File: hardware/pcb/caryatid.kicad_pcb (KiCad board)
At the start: 2 copper layers, 100 x 90 mm, 129 parts, among them J1 DC in, J10 FSR, J11 Digital bus, J12 RGB status, J13A Comms A - Qwiic, J13B Comms A - module, J14 Mic bias return, J15 Comms B - module, J16 Expansion / SPI1, J17 Audio out L/R/G, J18 Audio in L/R/rtn, J2 Battery, remote, J3 Latch switch, J4 Charge LEDs, J5 Analogue bus, J6 SW1 switch, J7 SW2 switch, J8 SW3 switch, J9 Soft pot, U1 BQ24074RGT, U2 TPS61023DRL, U3 74HC14, U4 MCP6002

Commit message: Hide back references, scope a clearance override to U1 and U2
Back-side designators hidden: 104 SMD parts at this density made them illegible
and they collided 87 times. JLC places from the CPL, not from silkscreen. Front
designators stay -- that face is sparse and is what a human cables up.

U1 and U2 get a footprint-level 0.15 mm clearance override. A 0.5 mm pitch
package fixes its own pad gaps and the HighCurrent netclass asks 0.3 mm, which
no land pattern at that pitch can meet. Scoped to the two packages; traces still
answer to their netclass.

Zone overflow now goes to the rescue pass rather than running off the board, and
the rescue pass keeps 3 mm of edge margin. R6, R9 and R10 were rescued; R10 had
been sitting exactly on the bottom edge.

Two bugs in my own insertion code, both of which produced a file that balanced
but was structurally wrong: the (hide yes) regex matched the closing paren of
the nested (font ...) rather than (effects ...), burying the flag inside the
font; and the clearance override silently matched nothing. Both replaced with
balanced-paren parsing.

silk_overlap 92 -> 5, clearance 18 -> 4, copper_edge_clearance 4 -> 0.
Non-ratsnest violations 133 -> 14.
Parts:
- moved R10 66.1 mm to (80.5, 56.5)
- moved R9 63.5 mm to (58.5, 56.5)
- moved R6 61.7 mm to (54.5, 56.5)

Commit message: Ground pour on F.Cu, and the boost hot loop
A GND zone on F.Cu, which that face can carry as a near-solid plane because it
holds only 21 through-hole parts. The zone ships unfilled -- kicad-cli has no
fill option -- so DRC reports the two GND vias as dangling until zones are
filled in the editor.

The hot loop: +5V_RAW from U2 pin 6 to C6 at 0.8 mm, and the return taken into
the plane by a via at each ground pad rather than by a track, so the return runs
directly under the outgoing current.

Two mistakes worth recording. A track wider than the pad pitch shorts to the
neighbouring pad -- 0.8 mm centred on pin 6 overlapped pin 5 -- so exits from
0.5 mm-pitch pads now neck to 0.25 mm and widen once clear. And via positions
are now searched against every back-side pad: the first attempt put a GND via
through C7's +5V pad, because I had checked it against the boost cluster only.

SW is left unrouted. U2 pin 5 can only exit right and C6 occupies that gap, so
there is no path to L1 at a useful width. That is placement, not routing: this
cluster has room for either the tight hot loop or the short SW node, not both.
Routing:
- net VOUT: track 0.00 -> 3.97 mm
- net +5V_RAW: track 0.00 -> 1.84 mm
- net GND: track 0.00 -> 1.00 mm, vias 0 -> 2
- added copper zone on F.Cu, net GND
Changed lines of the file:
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@@
+		)
+	)
+	(segment
+		(start 64.713 104.5)
+		(end 65.6 104.5)
+		(width 0.25)
+		(layer "B.Cu")
+		(net 4)
+	)
+	(segment
+		(start 65.6 104.5)
+		(end 66.55 104.5)
+		(width 0.8)
+		(layer "B.Cu")
+		(net 4)
+	)
+	(segment
+		(start 63.288 103.5)
+		(end 62.4 103.5)
+		(width 0.25)
+		(layer "B.Cu")
+		(net 94)
+	)
+	(segment
+		(start 62.4 103.5)
+		(end 61.45 103.5)
+		(width 1.2)
+		(layer "B.Cu")
+		(net 94)
+	)
+	(segment
+		(start 66.475 100.0)
+		(end 68.55 100.5)
+		(width 1.2)
+		(layer "B.Cu")
+		(net 94)
+	)
+	(segment
+		(start 68.45 104.5)
+		(end 68.95 104.5)
+		(width 0.25)
+		(layer "B.Cu")
+		(net 91)
+	)
+	(via
+		(at 68.95 104.5)
+		(size 0.6)
+		(drill 0.3)
+		(layers "F.Cu" "B.Cu")
+		(net 91)
+	)
+	(segment
+		(start 64.713 103.5)
+		(end 64.28 103.25)
+		(width 0.25)
+		(layer "B.Cu")
+		(net 91)
+	)
+	(via
+		(at 64.28 103.25)
+		(size 0.6)
+		(drill 0.3)
+		(layers "F.Cu" "B.Cu")
+		(net 91)
+	)
+	(zone
+		(net 91)
+		(net_name "GND")
+		(layer "F.Cu")
+		(name "GND plane")
+		(hatch edge 0.5)
+		(connect_pads
+			(clearance 0.3)
+		)
+		(min_thickness 0.25)
+		(filled_areas_thickness no)
+		(fill yes
+			(thermal_gap 0.3)
+			(thermal_bridge_width 0.5)
+		)
+		(polygon
+			(pts
+				(xy 50.6 30.6) (xy 149.4 30.6) (xy 149.4 119.4) (xy 50.6 119.4)
+			)
 		)
 	)

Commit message: Move C6 below U2 so SW routes
Putting the output cap beside U2 was the obvious spot and it quietly cost the
switching node: pin 5 can only exit right and C6 was standing in that gap. C6
now sits below U2, which frees the right side for L1 and, because pin 6 is on
the near edge either way, barely lengthens the hot loop.

  hot loop  1.84 -> 2.01 mm
  SW node   4.17 mm unroutable -> 2.31 mm, routed at 1.2 mm

Trading 0.17 mm of hot loop for a routable 1.5 A switching node is not close.
The general lesson is that routability is a placement constraint: optimising
loop length without it produced an arrangement that measured well and could not
be built.

Three power pins leave a 0.5 mm-pitch package into a 1.5 mm band, so every exit
necks to 0.2 mm and widens once clear of the pads. With that the routing adds no
DRC violations of its own -- the four clearance items are the pre-existing
SOT-563 pad-pitch ones against the 0.2 mm board floor.
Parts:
- moved R10 45.6 mm to (77.5, 102.0)
- moved R6 40.7 mm to (72.5, 93.0)
- moved R9 40.7 mm to (76.5, 93.0)
- moved R5 20.5 mm to (68.5, 93.0)
- moved C7 15.9 mm to (61.5, 96.0)
- moved FB1 8.32 mm to (64.5, 109.0)
- moved L1 5.32 mm to (68.5, 104.0)
- moved C5 4.95 mm to (73.0, 104.0)
- moved C6 4.03 mm to (64.0, 106.5), turned to 180 degrees
- moved R7 1.00 mm to (60.0, 106.5)
- moved R8 1.00 mm to (60.0, 108.5)
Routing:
- net /power/SW: track 0.00 -> 2.31 mm
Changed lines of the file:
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@@
 	(footprint "Capacitor_SMD:C_0805_2012Metric"
 		(layer "B.Cu")
-		(at 69.5 100.5)
+		(at 73.0 104.0)
 		(descr "Capacitor SMD 0805 (2012 Metric), square (rectangular) end terminal, IPC-7351 nominal, (Body size source: IPC-SM-782 page 76, https://www.pcb-3d.com/wordpress/wp-content/uploads/ipc-sm-782a_amendment_1_and_2.pdf, https://docs.google.com/spreadsheets/d/1BsfQQcO9C6DZCsRaXUlFlo91Tg2WpOkGARC1WS5S8t0/edit?usp=sharing), generated with kicad-footprint-generator")
 		(tags "capacitor")
@@
 	(footprint "Capacitor_SMD:C_0805_2012Metric"
 		(layer "B.Cu")
-		(at 67.5 104.5)
+		(at 64.0 106.5 180)
 		(descr "Capacitor SMD 0805 (2012 Metric), square (rectangular) end terminal, IPC-7351 nominal, (Body size source: IPC-SM-782 page 76, https://www.pcb-3d.com/wordpress/wp-content/uploads/ipc-sm-782a_amendment_1_and_2.pdf, https://docs.google.com/spreadsheets/d/1BsfQQcO9C6DZCsRaXUlFlo91Tg2WpOkGARC1WS5S8t0/edit?usp=sharing), generated with kicad-footprint-generator")
 		(tags "capacitor")
@@
 	(footprint "Capacitor_SMD:CP_Elec_6.3x5.4"
 		(layer "B.Cu")
-		(at 73.0 107.0)
+		(at 61.5 96.0)
 		(descr "SMD capacitor, aluminum electrolytic, Panasonic C55, 6.3x5.4mm")
 		(tags "capacitor electrolytic")
@@
 	(footprint "Inductor_SMD:L_0805_2012Metric"
 		(layer "B.Cu")
-		(at 71.5 104.5)
+		(at 64.5 109.0)
 		(descr "Inductor SMD 0805 (2012 Metric), square (rectangular) end terminal, IPC-7351 nominal, (Body size source: IPC-SM-782 page 80, https://www.pcb-3d.com/wordpress/wp-content/uploads/ipc-sm-782a_amendment_1_and_2.pdf), generated with kicad-footprint-generator")
 		(tags "inductor")
@@
 	(footprint "Inductor_SMD:L_Vishay_IFSC-1515AH_4x4x1.8mm"
 		(layer "B.Cu")
-		(at 65.0 100.0 180)
+		(at 68.5 104.0 180)
 		(descr "Low Profile, High Current Inductors (https://www.vishay.com/docs/34295/sc15ah01.pdf)")
 		(tags "SMD Vishay Inductor Low Profile")
@@
 	(footprint "Resistor_SMD:R_0603_1608Metric"
 		(layer "B.Cu")
-		(at 80.5 56.5)
+		(at 77.5 102.0)
 		(descr "Resistor SMD 0603 (1608 Metric), square (rectangular) end terminal, IPC-7351 nominal, (Body size source: IPC-SM-782 page 72, https://www.pcb-3d.com/wordpress/wp-content/uploads/ipc-sm-782a_amendment_1_and_2.pdf), generated with kicad-footprint-generator")
 		(tags "resistor")
@@
 	(footprint "Resistor_SMD:R_0603_1608Metric"
 		(layer "B.Cu")
-		(at 69.0 113.5)
+		(at 68.5 93.0)
 		(descr "Resistor SMD 0603 (1608 Metric), square (rectangular) end terminal, IPC-7351 nominal, (Body size source: IPC-SM-782 page 72, https://www.pcb-3d.com/wordpress/wp-content/uploads/ipc-sm-782a_amendment_1_and_2.pdf), generated with kicad-footprint-generator")
 		(tags "resistor")
@@
 	(footprint "Resistor_SMD:R_0603_1608Metric"
 		(layer "B.Cu")
-		(at 54.5 56.5)
+		(at 72.5 93.0)
 		(descr "Resistor SMD 0603 (1608 Metric), square (rectangular) end terminal, IPC-7351 nominal, (Body size source: IPC-SM-782 page 72, https://www.pcb-3d.com/wordpress/wp-content/uploads/ipc-sm-782a_amendment_1_and_2.pdf), generated with kicad-footprint-generator")
 		(tags "resistor")
@@
 	(footprint "Resistor_SMD:R_0603_1608Metric"
 		(layer "B.Cu")
-		(at 61.0 106.5)
+		(at 60.0 106.5)
 		(descr "Resistor SMD 0603 (1608 Metric), square (rectangular) end terminal, IPC-7351 nominal, (Body size source: IPC-SM-782 page 72, https://www.pcb-3d.com/wordpress/wp-content/uploads/ipc-sm-782a_amendment_1_and_2.pdf), generated with kicad-footprint-generator")
 		(tags "resistor")
@@
 	(footprint "Resistor_SMD:R_0603_1608Metric"
 		(layer "B.Cu")
-		(at 61.0 108.5)
+		(at 60.0 108.5)
 		(descr "Resistor SMD 0603 (1608 Metric), square (rectangular) end terminal, IPC-7351 nominal, (Body size source: IPC-SM-782 page 72, https://www.pcb-3d.com/wordpress/wp-content/uploads/ipc-sm-782a_amendment_1_and_2.pdf), generated with kicad-footprint-generator")
 		(tags "resistor")
@@
 	(footprint "Resistor_SMD:R_0603_1608Metric"
 		(layer "B.Cu")
-		(at 58.5 56.5)
+		(at 76.5 93.0)
 		(descr "Resistor SMD 0603 (1608 Metric), square (rectangular) end terminal, IPC-7351 nominal, (Body size source: IPC-SM-782 page 72, https://www.pcb-3d.com/wordpress/wp-content/uploads/ipc-sm-782a_amendment_1_and_2.pdf), generated with kicad-footprint-generator")
 		(tags "resistor")
@@
 	(segment
 		(start 64.713 104.5)
-		(end 65.6 104.5)
-		(width 0.25)
+		(end 64.713 105.5)
+		(width 0.2)
 		(layer "B.Cu")
 		(net 4)
 	)
 	(segment
-		(start 65.6 104.5)
-		(end 66.55 104.5)
+		(start 64.713 105.5)
+		(end 64.95 106.5)
 		(width 0.8)
 		(layer "B.Cu")
@@
 	)
 	(segment
+		(start 64.713 104.0)
+		(end 66.4 104.0)
+		(width 0.2)
+		(layer "B.Cu")
+		(net 50)
+	)
+	(segment
+		(start 66.4 104.0)
+		(end 67.025 104.0)
+		(width 1.2)
+		(layer "B.Cu")
+		(net 50)
+	)
+	(segment
 		(start 63.288 103.5)
-		(end 62.4 103.5)
-		(width 0.25)
+		(end 61.9 103.5)
+		(width 0.2)
 		(layer "B.Cu")
 		(net 94)
 	)
 	(segment
-		(start 62.4 103.5)
+		(start 61.9 103.5)
 		(end 61.45 103.5)
 		(width 1.2)
@@
 	)
 	(segment
-		(start 66.475 100.0)
-		(end 68.55 100.5)
+		(start 69.975 104.0)
+		(end 72.05 104.0)
 		(width 1.2)
 		(layer "B.Cu")
@@
 	)
 	(segment
-		(start 68.45 104.5)
-		(end 68.95 104.5)
-		(width 0.25)
+		(start 63.05 106.5)
+		(end 63.55 106.5)
+		(width 0.2)
 		(layer "B.Cu")
 		(net 91)
 	)
 	(via
-		(at 68.95 104.5)
+		(at 63.55 106.5)
 		(size 0.6)
 		(drill 0.3)
@@
 		(start 64.713 103.5)
 		(end 64.28 103.25)
-		(width 0.25)
+		(width 0.2)
 		(layer "B.Cu")
 		(net 91)

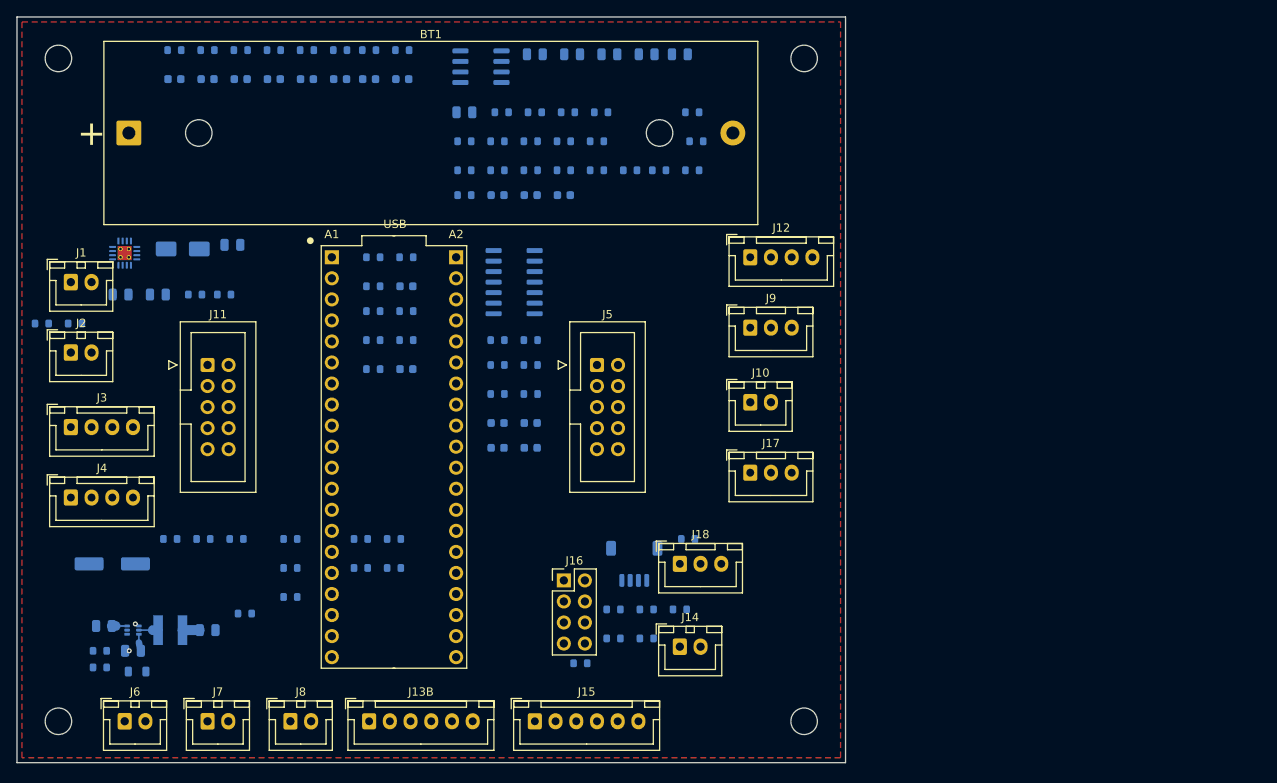
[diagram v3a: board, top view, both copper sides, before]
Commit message: Board to 150 x 90, and a checker for the constraints DRC misses
The recurring failure this session was always the same shape: a check that
modelled one thing and silently ignored another. tools/check_board.py now
enumerates all eight classes in one re-runnable pass -- courtyard overlap per
face INCLUDING the mounting holes, back parts over front through-hole pads,
outline margin, component height vs standoff, via annular ring, track width vs
pad pitch, and silkscreen against the fab floors. Four of those have no
equivalent in KiCad's DRC as configured, which is why they were all missed.

Outline 90 x 100 -> 150 x 90. Coverage 50% -> 33%, perimeter 380 -> 480 mm,
which matters because an early commit identified the perimeter rather than the
area as binding. All growth is on the long axis where the conservative BUD
rectangle leaves 15 mm; the 90 mm axis is untouched because it is the one proven
to fit. 100 x 150 was in the approved plan and is NOT what was built -- 100
exceeds the documented 95.2 mm BUD width, which the plan failed to check.

Three DRC rules were set looser than the fab and reported false passes:
min_via_annular_width 0.13 -> 0.18, min_hole_to_hole 0.25 -> 0.45. min_clearance
0.20 -> 0.15, still 1.5x JLC's 0.10, which retires the four SOT-563 clearance
errors caused by its own pad pitch.

Via pads 0.55/0.6 -> 0.70 on 0.3 drill for a 0.20 mm ring; QFN thermal vias
inboard to +/-0.45 so the larger pad still clears the signal pads by 0.25 mm.

Standoffs are 7 mm, set by C7 at 5.4 mm on the back face. The height was never
specified and 4-5 mm does not clear it -- found by the user, not by me, which is
why the height check now exists.

ADR 0008 records the outline and layer count, which were never written up
despite ADR 0001's own criterion. It also retires the 'neither edge past 100 mm'
rule: the price tier is real but the cost of crossing it was never checked, and
checking it showed the increase is small.

DRC non-ratsnest 14 -> 10. ERC 0. Pin map unchan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
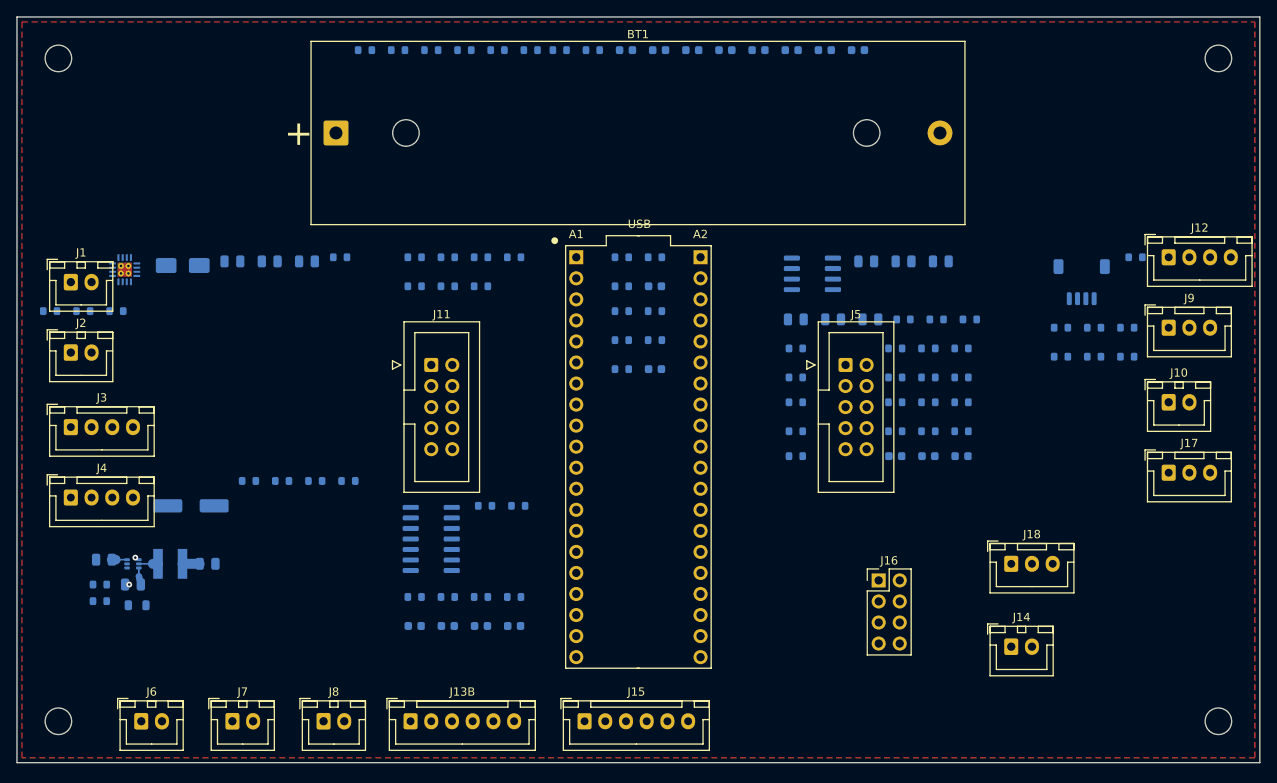
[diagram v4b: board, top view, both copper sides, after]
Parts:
- moved R46 75.7 mm to (184.0, 71.0)
- moved J13A 63.8 mm to (178.5, 62.0)
- moved R40 63.8 mm to (185.0, 59.0)
- moved R41 63.8 mm to (176.0, 67.5)
- moved R42 63.8 mm to (180.0, 67.5)
- moved R43 63.8 mm to (184.0, 67.5)
- moved R44 63.8 mm to (176.0, 71.0)
- moved R45 63.8 mm to (180.0, 71.0)
- moved R52 61.3 mm to (160.0, 70.0)
- moved R53 61.3 mm to (164.0, 70.0)
- moved C23 57.4 mm to (156.0, 83.0)
- moved C27 57.4 mm to (160.0, 83.0)
- moved C30 57.4 mm to (164.0, 83.0)
- moved R59 55.6 mm to (156.0, 76.5)
- moved R60 55.6 mm to (160.0, 76.5)
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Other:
- board size 100 x 90 mm -> 150 x 90 mm
- board text added: "caryatid 150 x 90 mm 2 layer"
- board text removed: "caryatid 90 x 100 mm 2 layer"

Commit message: Everything to the front; ground plane to B.Cu; standoff 2 mm
The enclosure is shallow, so the standoff has to be short, and C7 at 5.4 mm
cannot hang under it. Rather than move the tall parts individually, every
component moves to the front. That fixes three things at once: the standoff drops
7 mm -> 2 mm (stack ~30 -> ~25), SMT returns to single-sided and therefore
Economic, and B.Cu is freed as a routing layer instead of carrying 104 parts and
141 signals. The ground pour moves to B.Cu, which is now genuinely empty.

This reverses the SMD-to-back flip. That was right at 90 x 100, where reclaiming
the copper under the cell mattered; at 150 x 90 it does not, and a short standoff
outranks it.

Three bugs the move exposed, all the same shape -- something tuned to the old
arrangement that nothing re-derived:

Moving a part between faces MIRRORS its pin layout vertically. U2's pin 6 sat
below centre on B.Cu and sits above it on F.Cu, so every y offset in the boost
cluster had to flip. The relative arrangement is unchanged; only the sign is.

The escape routes carried absolute x targets tuned to the cluster's old position.
Moving U2 from x 14 to x 26 turned each one into an 11-13 mm track running
backwards across the board, shorting four nets. They are deltas now.

place_board.py's own collision checks split parts by is_smd(), which stopped
meaning front/back the moment everything moved to one face. check_board.py reads
the board itself and caught what the placer could not see -- which is the whole
reason it exists.

J2 is untouched. Removing it is reasonable for this build but forecloses a remote
pack for absonus and baby borg, and that is ADR 0002's call to make, not mine.

DRC non-ratsnest 10 -> 9. ERC 0. All eight custom checks pass. Pin map unchanged.
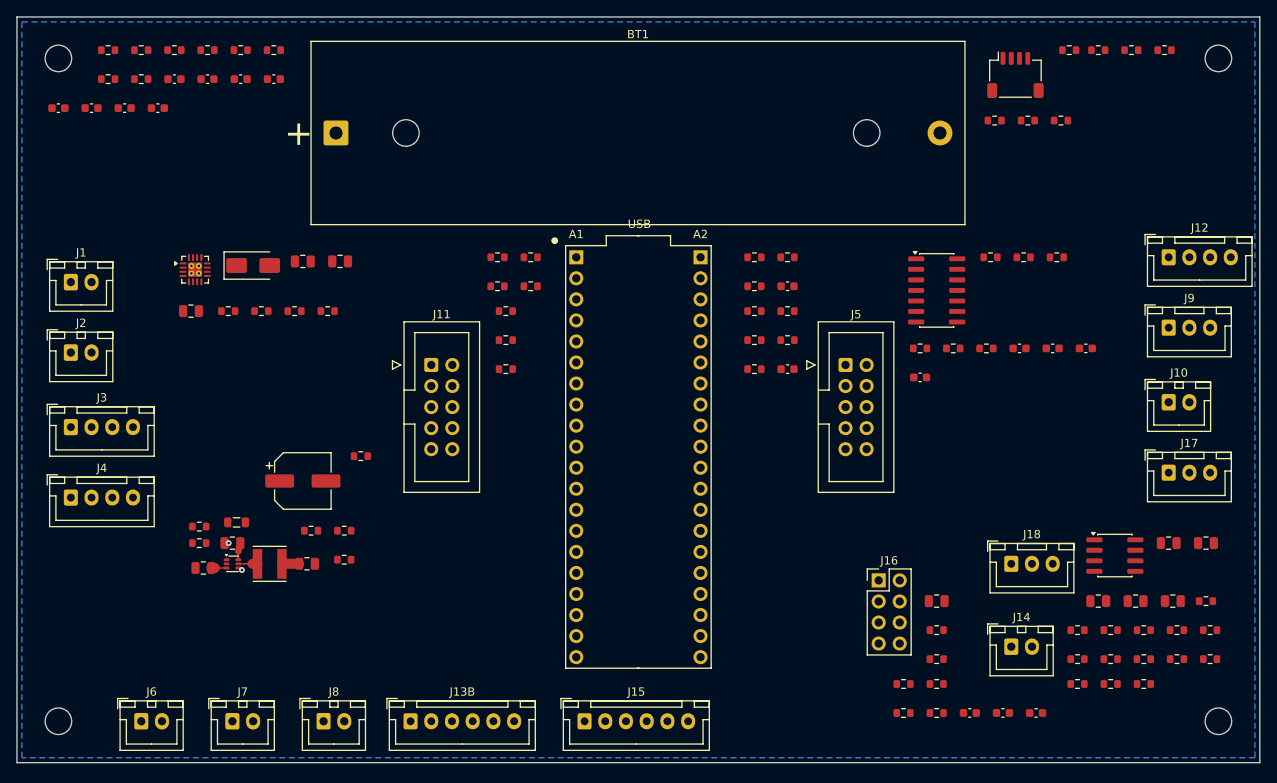
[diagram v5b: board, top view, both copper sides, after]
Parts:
- C1, C10, C11, C12, C13, C14, C15, C16, C17, C18, C19, C2, C20, C21, C22, C23, C24, C25, C26, C27, C28, C29, C3, C30, C4, C5, C6, C7, C8, C9, D1, FB1, J13A, L1, R1, R10, R11, R12, R13, R14, R15, R16, R17, R18, R19, R2, R20, R21, R22, R23, R24, R25, R26, R27, R28, R29, R3, R30, R31, R32, R33, R34, R35, R36, R37, R38, R39, R4, R40, R41, R42, R43, R44, R45, R46, R47, R48, R49, R5, R50, R51, R52, R53, R54, R55, R56, R57, R58, R59, R6, R60, R61, R62, R63, R64, R65, R66, R7, R8, R9, U1, U2, U3, U4: moved to F.Cu
- moved R36 87.7 mm to (175.5, 59.0)
- moved C14 84.8 mm to (55.0, 41.0)
- moved C15 84.8 mm to (59.0, 41.0)
- moved C16 84.8 mm to (63.0, 41.0)
- moved C17 84.8 mm to (67.0, 41.0)
- moved C18 80.3 mm to (171.0, 70.0)
- moved C19 80.3 mm to (175.0, 70.0)
- moved C20 80.3 mm to (179.0, 70.0)
- moved R34 68.0 mm to (167.5, 59.0)
- moved R35 68.0 mm to (171.5, 59.0)
- moved U3 68.0 mm to (161.0, 63.0)
- moved R37 64.4 mm to (159.0, 70.0)
- moved R38 64.4 mm to (163.0, 70.0)
- moved R39 64.4 mm to (167.0, 70.0)
- moved C21 57.5 mm to (159.0, 73.5)
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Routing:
- added copper zone on B.Cu, net GND
- removed copper zone on F.Cu, net GND
